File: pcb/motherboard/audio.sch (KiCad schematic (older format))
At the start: 34 parts, among them J10 DF13A-10DP-1.25V, J13 DOUT, J14 VOUT-R, J15 GND, U7 PCM2704C, U8 TPA2005, Y1 12.00 Mhz

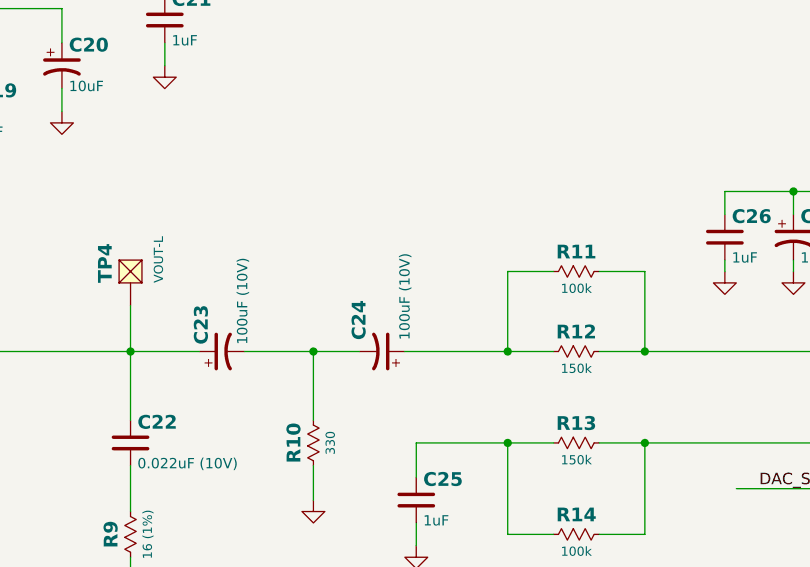
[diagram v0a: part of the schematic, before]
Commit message: Fixed wrong cap value for C24 and part # for C7,C9
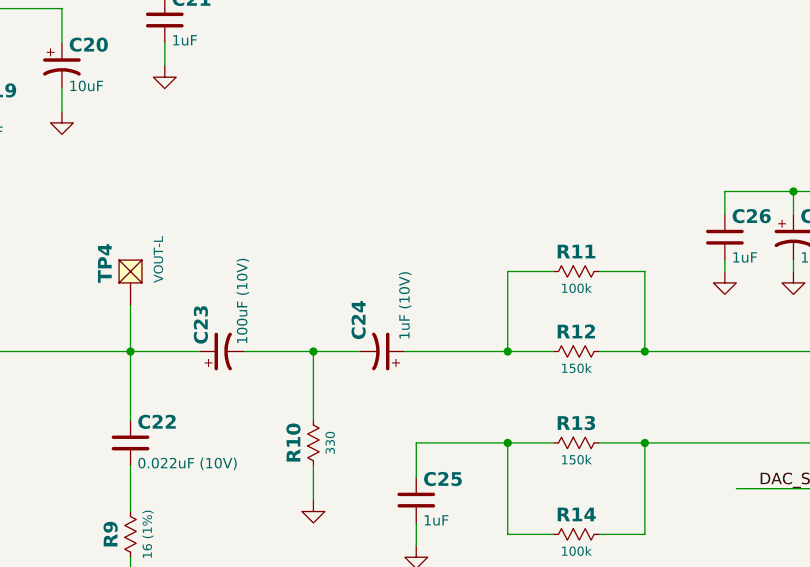
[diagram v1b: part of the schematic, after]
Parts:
- C24: value 100uF (10V) -> 1uF (10V)
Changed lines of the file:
@@
 P 6600 4750
 F 0 "C24" H 6650 4650 60  0000 L CNB
-F 1 "100uF (10V)" H 6650 4850 45  0000 L CNN
+F 1 "1uF (10V)" H 6650 4850 45  0000 L CNN
 F 2 "SMT:CPL-0805" H 6635 4595 40  0001 L CNN
 F 3 "" H 6600 4850 60  0000 C CNN
